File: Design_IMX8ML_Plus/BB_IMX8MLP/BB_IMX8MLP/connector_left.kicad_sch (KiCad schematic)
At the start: 4 parts, among them J3 Front_Left, J4 Back_Left

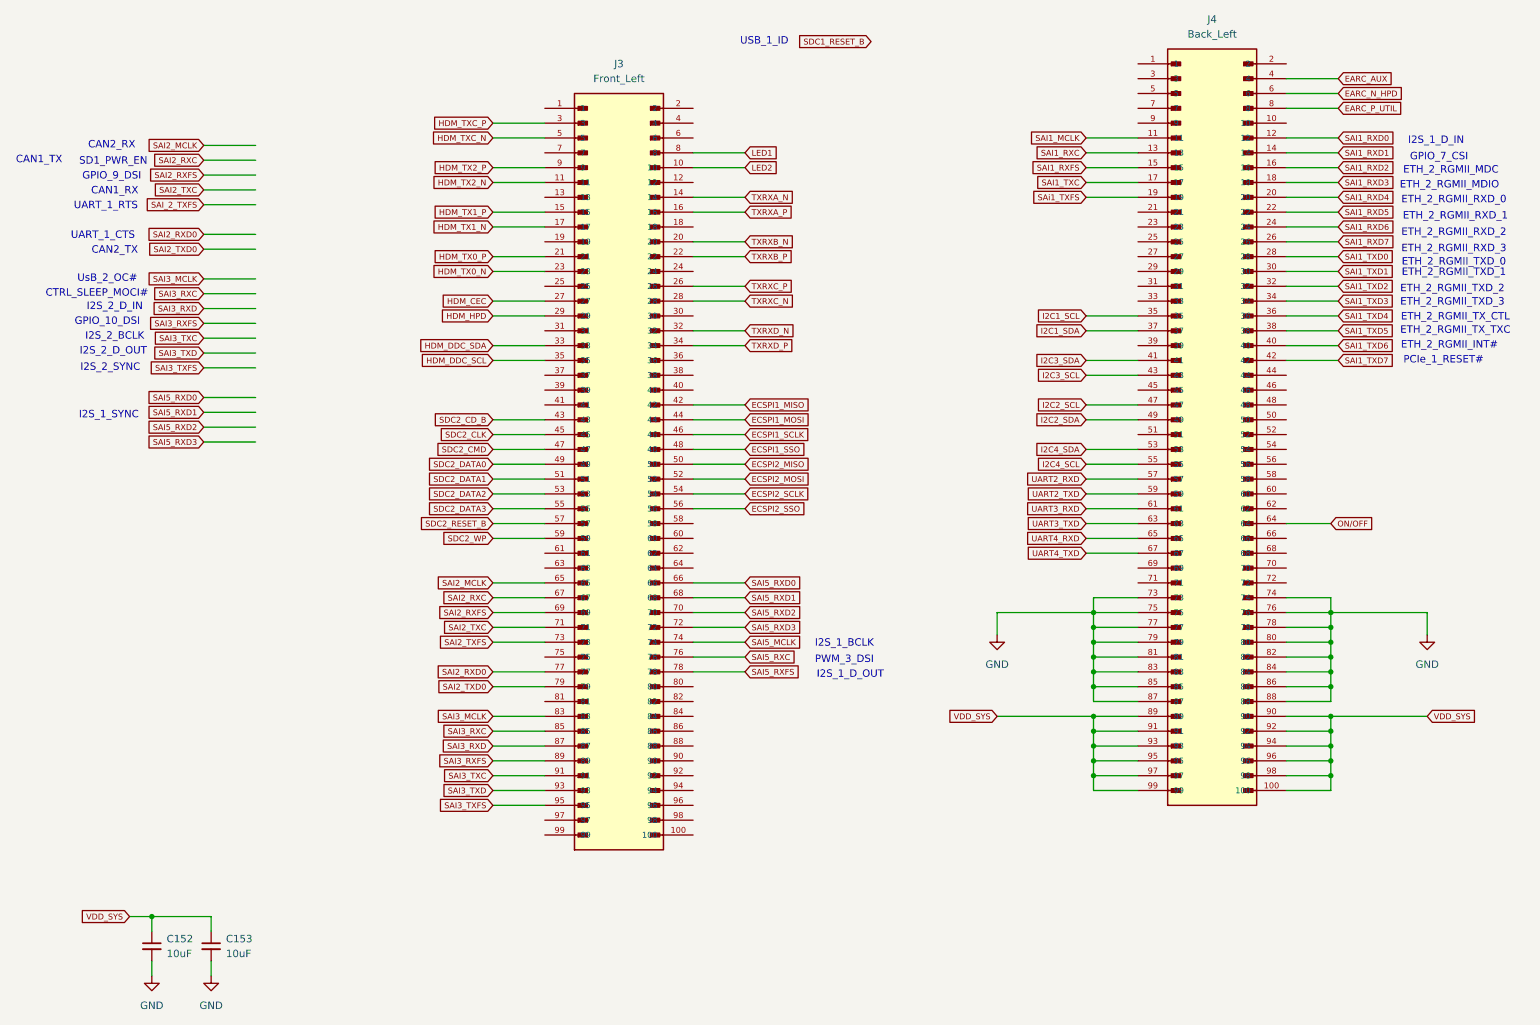
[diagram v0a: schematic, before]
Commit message: [PROCESSOR] Create zones It added power zones in the four layer
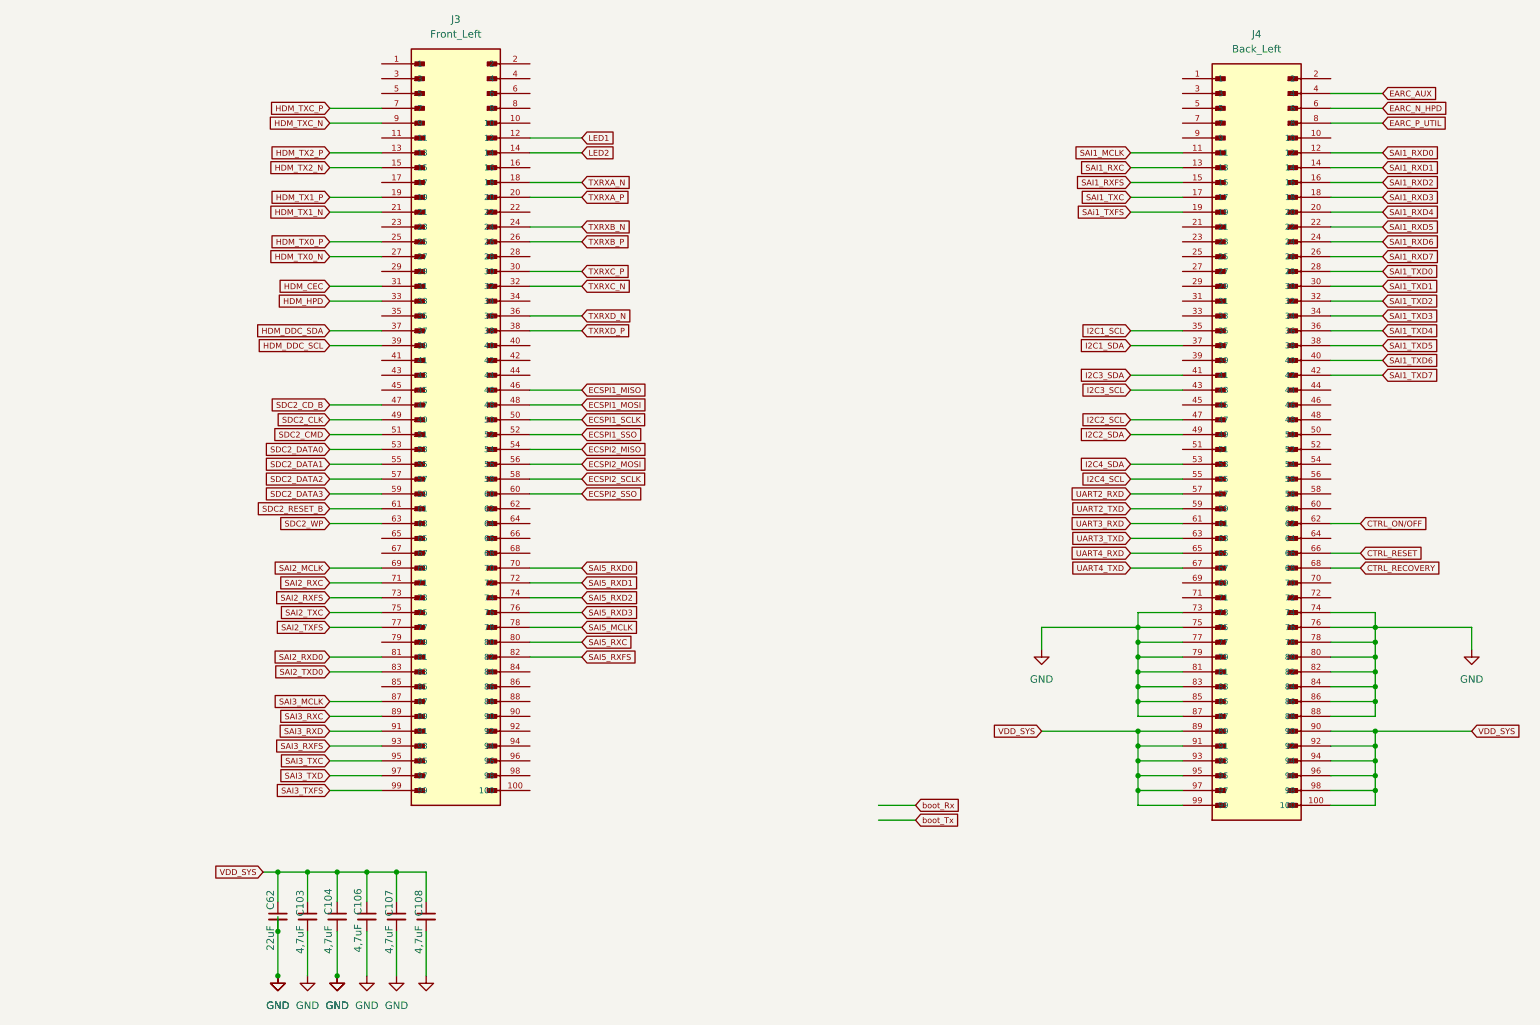
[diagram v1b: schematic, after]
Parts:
- removed C152, C153: 10uF, Capacitor_SMD:C_0603_1608Metric, symbol Device:C_Small
- added C103, C104, C106, C107, C108: 4,7uF, Capacitor_SMD:C_0402_1005Metric, symbol Device:C_Small
- added C62: 22uF, Capacitor_SMD:C_0402_1005Metric, symbol Device:C_Small
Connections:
- net ECSPI1_MISO: now also J3.46; no longer J3.42
- net ECSPI1_MOSI: now also J3.48; no longer J3.44
- net ECSPI1_SCLK: now also J3.50; no longer J3.46
- net ECSPI1_SSO: now also J3.52; no longer J3.48
- net ECSPI2_MISO: now also J3.54; no longer J3.50
- net ECSPI2_MOSI: now also J3.56; no longer J3.52
- net ECSPI2_SCLK: now also J3.58; no longer J3.54
- net ECSPI2_SSO: now also J3.60; no longer J3.56
- net GND: now also C103.2, C104.2, C106.2, C107.2, C108.2, C62.2
- net HDM_CEC: now also J3.31; no longer J3.27
- net HDM_DDC_SCL: now also J3.39; no longer J3.35
- net HDM_DDC_SDA: now also J3.37; no longer J3.33
- net HDM_HPD: now also J3.33; no longer J3.29
- net HDM_TX0_N: now also J3.27; no longer J3.23
- net HDM_TX0_P: now also J3.25; no longer J3.21
- net HDM_TX1_N: now also J3.21; no longer J3.17
- net HDM_TX1_P: now also J3.19; no longer J3.15
- net HDM_TX2_N: now also J3.15; no longer J3.11
- net HDM_TX2_P: now also J3.13; no longer J3.9
- net HDM_TXC_N: now also J3.9; no longer J3.5
- net HDM_TXC_P: now also J3.7; no longer J3.3
- net LED1: now also J3.12; no longer J3.8
- net LED2: now also J3.14; no longer J3.10
- net SAI2_MCLK: now also J3.69; no longer J3.65
- net SAI2_RXC: now also J3.71; no longer J3.67
- net SAI2_RXD0: now also J3.81; no longer J3.77
- net SAI2_RXFS: now also J3.73; no longer J3.69
- net SAI2_TXC: now also J3.75; no longer J3.71
- net SAI2_TXD0: now also J3.83; no longer J3.79
- net SAI2_TXFS: now also J3.77; no longer J3.73
- net SAI3_MCLK: now also J3.87; no longer J3.83
- net SAI3_RXC: now also J3.89; no longer J3.85
- net SAI3_RXD: now also J3.91; no longer J3.87
- net SAI3_RXFS: now also J3.93; no longer J3.89
- net SAI3_TXC: now also J3.95; no longer J3.91
- net SAI3_TXD: now also J3.97; no longer J3.93
- net SAI3_TXFS: now also J3.99; no longer J3.95
- net SAI5_MCLK: now also J3.78; no longer J3.74
- net SAI5_RXC: now also J3.80; no longer J3.76
- net SAI5_RXD0: now also J3.70; no longer J3.66
- net SAI5_RXD1: now also J3.72; no longer J3.68
- net SAI5_RXD2: now also J3.74; no longer J3.70
- net SAI5_RXD3: now also J3.76; no longer J3.72
- net SAI5_RXFS: now also J3.82; no longer J3.78
- net SDC2_CD_B: now also J3.47; no longer J3.43
- net SDC2_CLK: now also J3.49; no longer J3.45
- net SDC2_CMD: now also J3.51; no longer J3.47
- net SDC2_DATA0: now also J3.53; no longer J3.49
- net SDC2_DATA1: now also J3.55; no longer J3.51
- net SDC2_DATA2: now also J3.57; no longer J3.53
- net SDC2_DATA3: now also J3.59; no longer J3.55
- net SDC2_RESET_B: now also J3.61; no longer J3.57
- net SDC2_WP: now also J3.63; no longer J3.59
- net TXRXA_N: now also J3.18; no longer J3.14
- net TXRXA_P: now also J3.20; no longer J3.16
- net TXRXB_N: now also J3.24; no longer J3.20
- net TXRXB_P: now also J3.26; no longer J3.22
- net TXRXC_N: now also J3.32; no longer J3.28
- net TXRXC_P: now also J3.30; no longer J3.26
- net TXRXD_N: now also J3.36; no longer J3.32
- net TXRXD_P: now also J3.38; no longer J3.34
- net VDD_SYS: now also C103.1, C104.1, C106.1, C107.1, C108.1, C62.1
- net CTRL_ON/OFF: now reaches J4.62
- net CTRL_RESET: now reaches J4.66
- net CTRL_RECOVERY: now reaches J4.68
- net ON/OFF: no longer names the net of J4.64
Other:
- note removed: "CAN1_RX"
- note removed: "CAN1_TX"
- note removed: "CAN2_RX"
- note removed: "CAN2_TX"
- note removed: "CTRL_SLEEP_MOCI#"
- note removed: "ETH_2_RGMII_INT#"
- note removed: "ETH_2_RGMII_MDC"
- note removed: "ETH_2_RGMII_MDIO"
- note removed: "ETH_2_RGMII_RXD_0"
- note removed: "ETH_2_RGMII_RXD_1"
- note removed: "ETH_2_RGMII_RXD_2"
- note removed: "ETH_2_RGMII_RXD_3"
- note removed: "ETH_2_RGMII_TXD_0"
- note removed: "ETH_2_RGMII_TXD_1"
- note removed: "ETH_2_RGMII_TXD_2"
- note removed: "ETH_2_RGMII_TXD_3"
- note removed: "ETH_2_RGMII_TX_CTL"
- note removed: "ETH_2_RGMII_TX_TXC"
- note removed: "GPIO_10_DSI"
- note removed: "GPIO_7_CSI"
- note removed: "GPIO_9_DSI"
- note removed: "I2S_1_BCLK"
- note removed: "I2S_1_D_IN"
- note removed: "I2S_1_D_OUT"
- note removed: "I2S_1_SYNC"
- note removed: "I2S_2_BCLK"
- note removed: "I2S_2_D_IN"
- note removed: "I2S_2_D_OUT"
- note removed: "I2S_2_SYNC"
- note removed: "PCIe_1_RESET#"
- note removed: "PWM_3_DSI"
- note removed: "SD1_PWR_EN"
- note removed: "UART_1_CTS"
- note removed: "UART_1_RTS"
- note removed: "USB_1_ID"
- note removed: "UsB_2_OC#"
- moved on the sheet: J3
